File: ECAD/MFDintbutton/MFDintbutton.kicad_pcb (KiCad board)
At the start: 2 copper layers, 113 x 113 mm, 41 parts, among them J1 Conn_02x03_Odd_Even, J2 Conn_01x04, J3 Conn_01x04, J4 Conn_01x04, SW11 SW_Push, SW12 SW_Push, SW13 SW_Push, SW14 SW_Push, SW21 SW_Push, SW22 SW_Push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

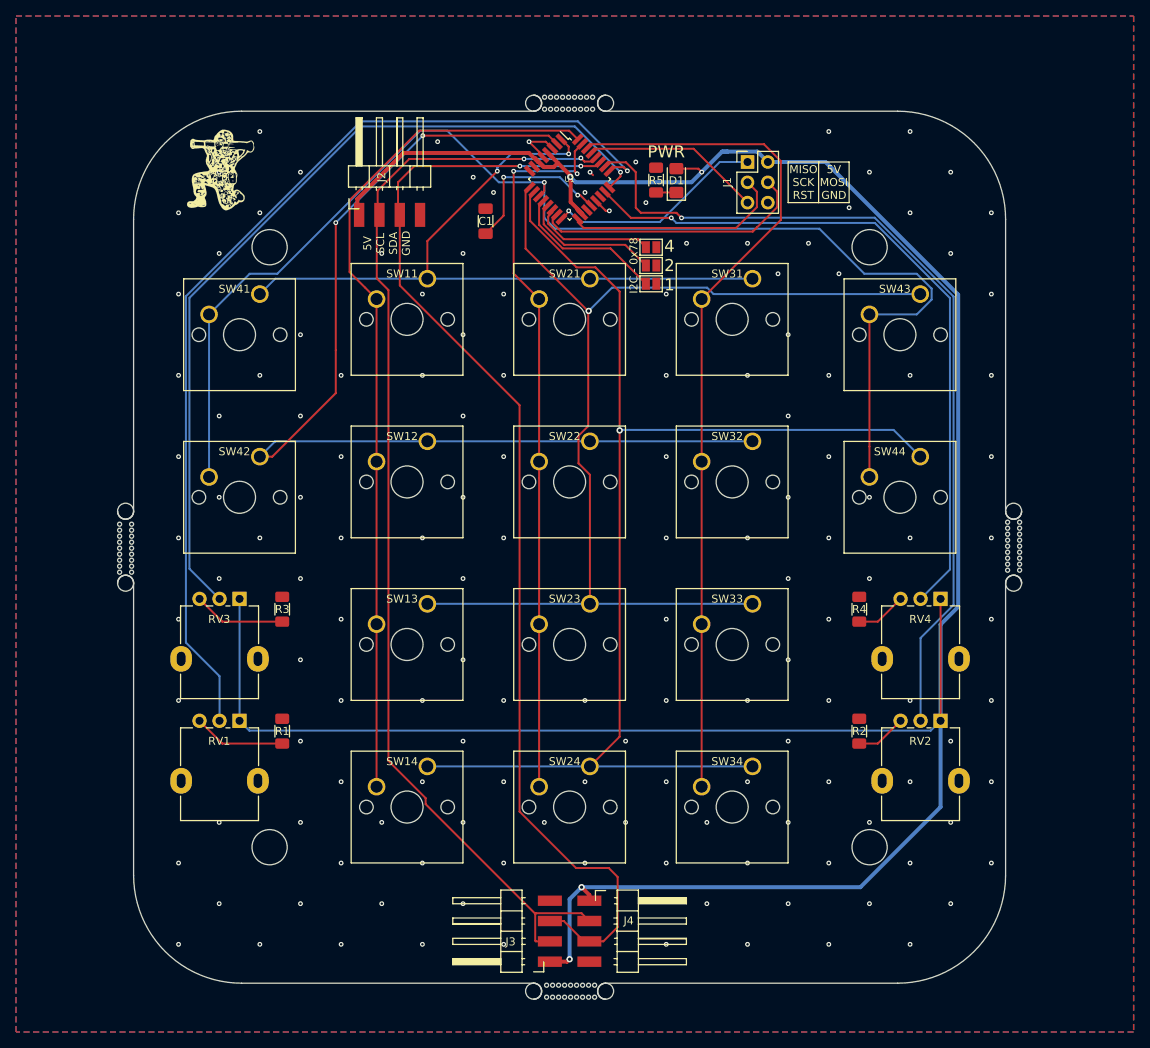
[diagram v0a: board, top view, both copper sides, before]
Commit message: Removing panelisations, adding polyfuses
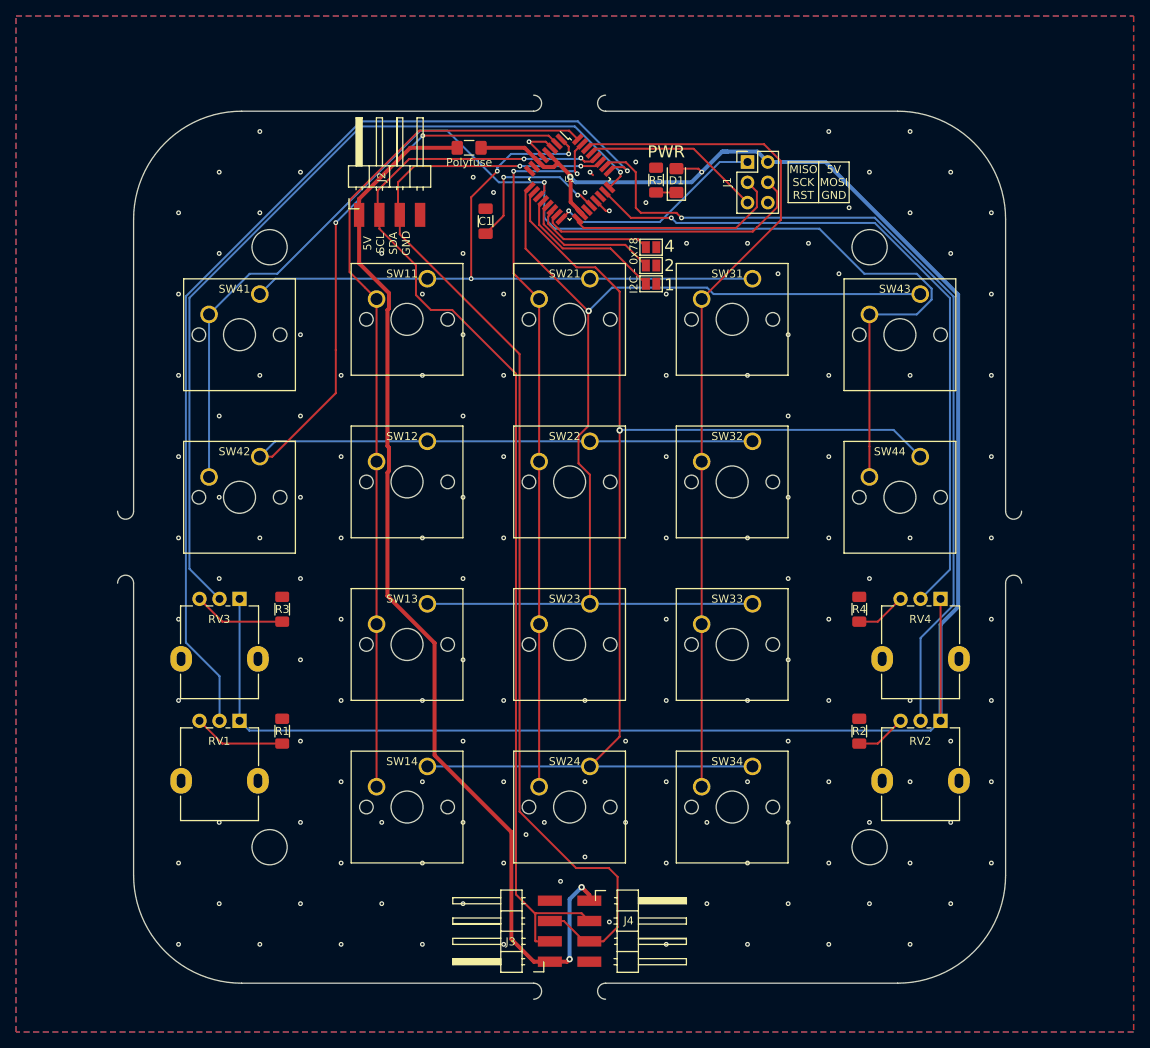
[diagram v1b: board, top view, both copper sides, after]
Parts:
- removed G***: LOGO, mycustomlibrary:puff_1200
- removed G***: LOGO, mycustomlibrary:CBB_0.5inch
- removed mouse-bite-2mm-slot (x4): VAL**, Panelisation:mouse-bite-2mm-slot-5mm-width
- added Polyfuse: Polyfuse, Fuse:Fuse_1206_3216Metric_Pad1.42x1.75mm_HandSolder, F.Cu at (43.9, 4.57)
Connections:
- J2 pad 1: +5V -> Net-(F1-Pad2)
- J3 pad 1: +5V -> Net-(F1-Pad2)
- J4 pad 1: +5V -> Net-(F1-Pad2)
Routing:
- net Net-(F1-Pad2): track 0.00 -> 135.9 mm, vias 0 -> 2
- net +5V: track 349.9 -> 256.3 mm, vias 4 -> 2
- net /ROW1: track 91.7 -> 89.3 mm, vias 2 -> 3
- net SCL: track 140.5 -> 141.8 mm
- net GND: vias 147 -> 148

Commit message: Change from 1x04 2.54mm headers to 1x05 micro JST
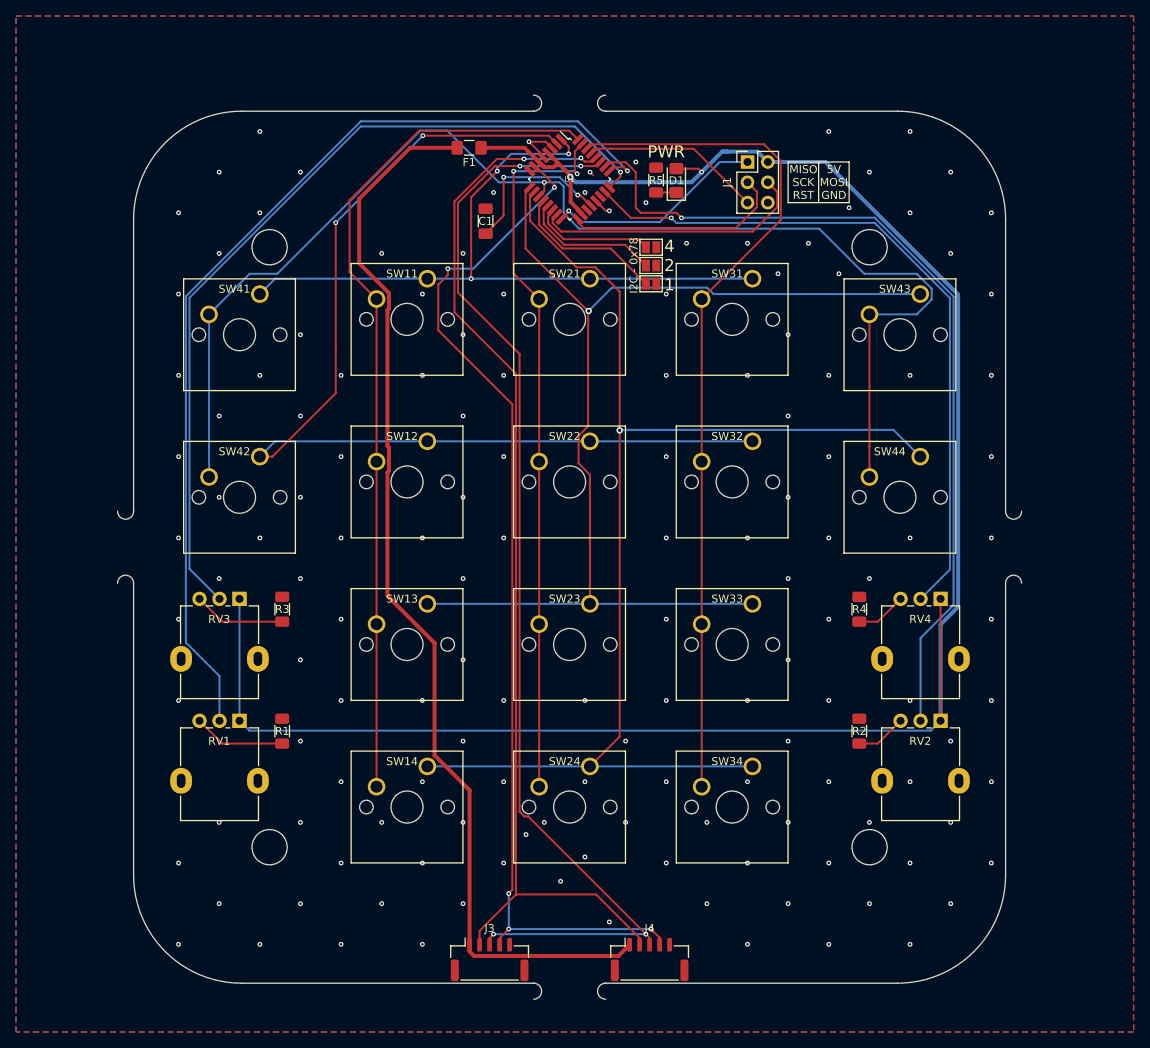
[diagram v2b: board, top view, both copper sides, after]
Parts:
- removed J2: Conn_01x04, mycustomlibrary:PinHeader_1x04_P2.54mm_Horizontal_SMD
- J3, J4: value Conn_01x04 -> Conn_01x05; footprint mycustomlibrary:PinHeader_1x04_P2.54mm_Horizontal_SMD -> Connector_JST:JST_GH_SM05B-GHS-TB_1x05-1MP_P1.25mm_Horizontal
- moved J3 6.54 mm to (46.5, 106.0), turned to 0 degrees
- moved J4 6.54 mm to (66.5, 106.0)
- renumbered Polyfuse to F1
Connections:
- J3 pad 4: GND -> /BUS_SIGNAL
- J4 pad 4: GND -> /BUS_SIGNAL
- U1 pad 7: Net-(U1-Pad7) -> /BUS_SIGNAL
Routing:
- net /BUS_SIGNAL: track 0.00 -> 131.0 mm, vias 0 -> 5
- net SCL: track 141.8 -> 136.9 mm
- net /COL4: track 163.2 -> 162.6 mm
- net Net-(F1-Pad2): track 135.9 -> 135.8 mm, vias 2 -> 0
- net SDA: vias 2 -> 4
- net GND: vias 148 -> 145
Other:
- board text removed: "5V SCL SDA GND"

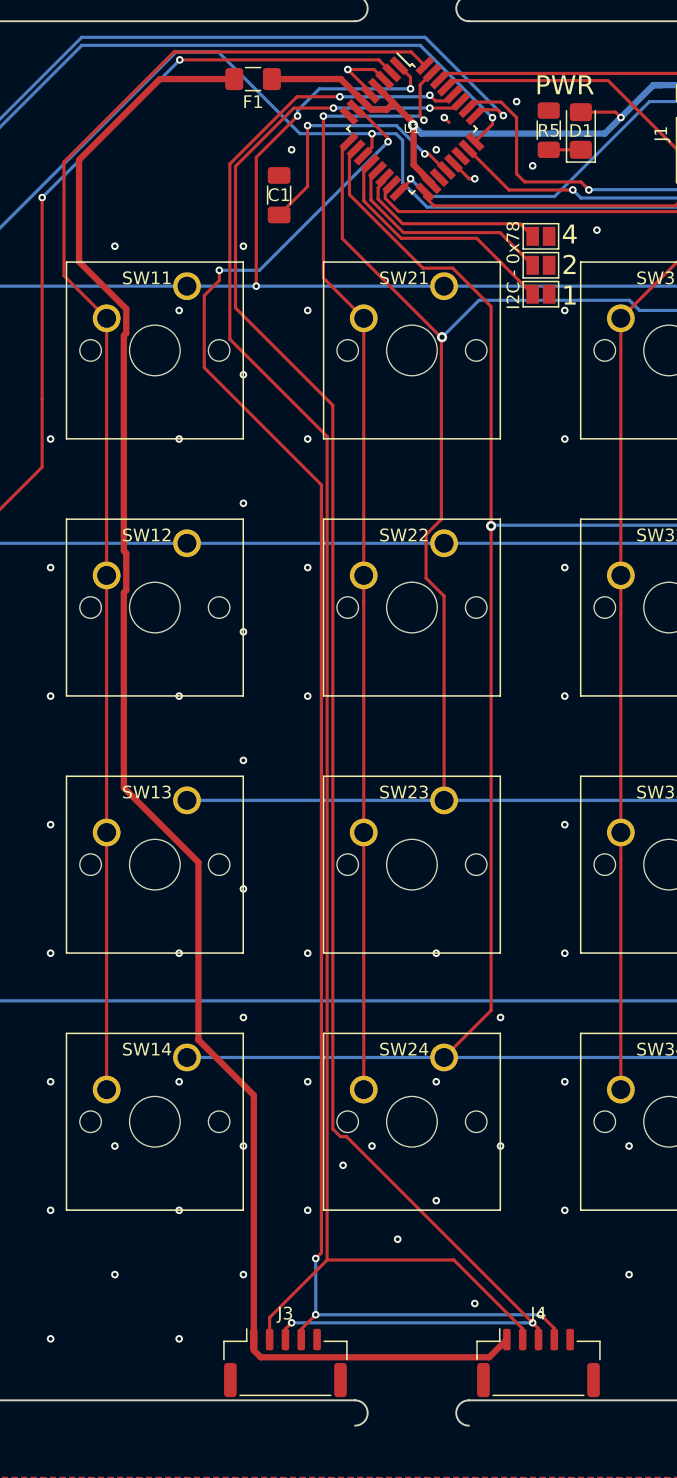
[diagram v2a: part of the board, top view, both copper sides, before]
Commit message: Swap bus connector to 4-pin JST-GH
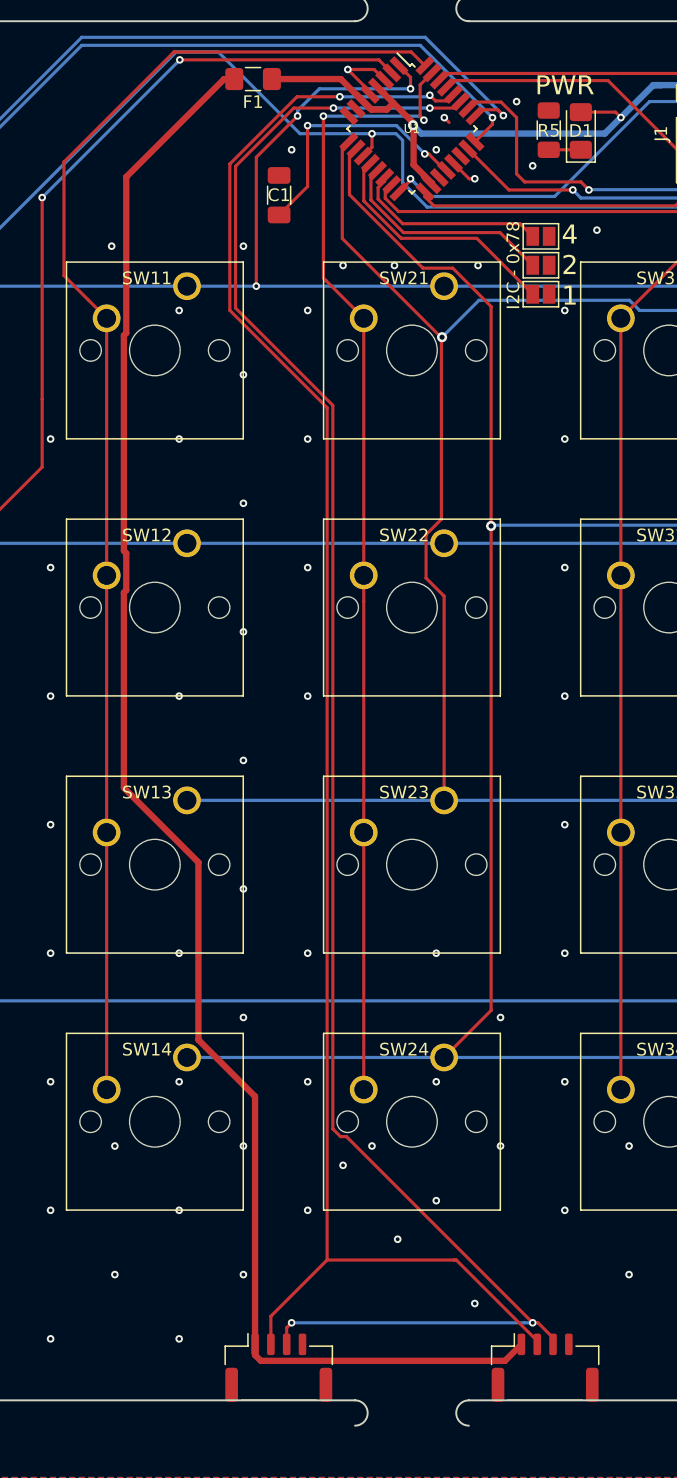
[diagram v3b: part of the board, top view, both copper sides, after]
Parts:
- removed J4: Conn_01x05, Connector_JST:JST_GH_SM05B-GHS-TB_1x05-1MP_P1.25mm_Horizontal
- added J2: Conn_01x04, Connector_JST:JST_GH_SM04B-GHS-TB_1x04-1MP_P1.25mm_Horizontal, F.Cu at (46.0, 106.4)
- J3: value Conn_01x05 -> Conn_01x04; footprint Connector_JST:JST_GH_SM05B-GHS-TB_1x05-1MP_P1.25mm_Horizontal -> Connector_JST:JST_GH_SM04B-GHS-TB_1x04-1MP_P1.25mm_Horizontal
- moved J3 20.5 mm to (67.0, 106.4)
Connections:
- J3 pad 4: /BUS_SIGNAL -> GND
- U1 pad 7: /BUS_SIGNAL -> Net-(U1-Pad7)
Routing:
- net /BUS_SIGNAL: track 131.0 -> 0.00 mm, vias 5 -> 0
- net Net-(F1-Pad2): track 135.8 -> 131.2 mm
- net SDA: track 143.4 -> 144.9 mm
- net SCL: track 136.9 -> 138.2 mm
- net GND: vias 145 -> 148

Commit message: major update, MCAD and some programs
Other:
- board size 113 x 113 mm -> 109 x 109 mm
